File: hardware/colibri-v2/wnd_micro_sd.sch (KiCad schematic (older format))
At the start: 12 parts

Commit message: Added footprints
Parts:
- removed MSD1: uSDCARD-H1.85, symbol uSDCARD-H1.85
- added MSD1: WURTH_693071010811, Sigmadrone:WURTH_693071010811, symbol WURTH_693071010811
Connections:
- wire segments 40 -> 37
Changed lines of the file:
@@
 $Descr A4 11693 8268
 encoding utf-8
-Sheet 13 28
+Sheet 12 28
 Title ""
 Date ""
@@
 Comment4 ""
 $EndDescr
-$Comp
-L uSDCARD-H1.85 MSD1
-U 1 1 56153956
-P 6350 4000
-F 0 "MSD1" H 6600 3300 60  0000 C CNN
-F 1 "uSDCARD-H1.85" H 6450 4700 60  0000 C CNN
-F 2 "" H 6350 4000 60  0001 C CNN
-F 3 "" H 6350 4000 60  0000 C CNN
-	1    6350 4000
-	1    0    0    -1
-$EndComp
 Text HLabel 3450 3450 0    60   BiDi ~ 0
 SD1_DATA2
@@
 SD1_WP
 $Comp
-L GND #PWR108
+L GND #PWR0114
 U 1 1 5617363A
 P 5350 5200
-F 0 "#PWR108" H 5350 4950 50  0001 C CNN
+F 0 "#PWR0114" H 5350 4950 50  0001 C CNN
 F 1 "GND" H 5350 5050 50  0000 C CNN
 F 2 "" H 5350 5200 60  0000 C CNN
@@
 	1    0    0    -1
 $EndComp
-$Comp
-L GND #PWR109
-U 1 1 5617364F
-P 6100 5200
-F 0 "#PWR109" H 6100 4950 50  0001 C CNN
-F 1 "GND" H 6100 5050 50  0000 C CNN
-F 2 "" H 6100 5200 60  0000 C CNN
-F 3 "" H 6100 5200 60  0000 C CNN
-	1    6100 5200
-	1    0    0    -1
-$EndComp
 Wire Wire Line
 	5500 4550 5350 4550
 Wire Wire Line
 	5350 3950 5350 5200
-Wire Wire Line
-	6100 4850 6100 5200
-Wire Wire Line
-	6200 4850 6200 4950
-Wire Wire Line
-	6200 4950 6100 4950
-Connection ~ 6100 4950
 Wire Wire Line
 	3450 3450 5500 3450
@@
 	3800 3850 3450 3850
 $Comp
-L +3V3 #PWR107
+L +3V3 #PWR0115
 U 1 1 561737FF
 P 5350 1550
-F 0 "#PWR107" H 5350 1400 50  0001 C CNN
+F 0 "#PWR0115" H 5350 1400 50  0001 C CNN
 F 1 "+3V3" H 5350 1690 50  0000 C CNN
 F 2 "" H 5350 1550 60  0000 C CNN
@@
 	4200 4450 4200 4600
 $Comp
-L GND #PWR106
+L GND #PWR0116
 U 1 1 56173E31
 P 4200 5200
-F 0 "#PWR106" H 4200 4950 50  0001 C CNN
+F 0 "#PWR0116" H 4200 4950 50  0001 C CNN
 F 1 "GND" H 4200 5050 50  0000 C CNN
 F 2 "" H 4200 5200 60  0000 C CNN
@@
 Connection ~ 4900 1850
 $Comp
-L GND #PWR110
+L GND #PWR0117
 U 1 1 5617463C
 P 6500 2850
-F 0 "#PWR110" H 6500 2600 50  0001 C CNN
+F 0 "#PWR0117" H 6500 2600 50  0001 C CNN
 F 1 "GND" H 6500 2700 50  0000 C CNN
 F 2 "" H 6500 2850 60  0000 C CNN
@@
 	5500 4450 5350 4450
 Connection ~ 5350 4450
+$Comp
+L WURTH_693071010811 MSD1
+U 1 1 56D6C0E1
+P 6350 4000
+F 0 "MSD1" H 6600 3300 60  0000 C CNN
+F 1 "WURTH_693071010811" H 6450 4700 60  0000 C CNN
+F 2 "Sigmadrone:WURTH_693071010811" H 6350 4000 60  0001 C CNN
+F 3 "" H 6600 3300 60  0000 C CNN
+F 4 "2081363" H 6400 4900 60  0001 C CNN "Part"
+F 5 "Farnell" H 6400 4800 60  0001 C CNN "Provider"
+	1    6350 4000
+	1    0    0    -1
+$EndComp
 $EndSCHEMATC

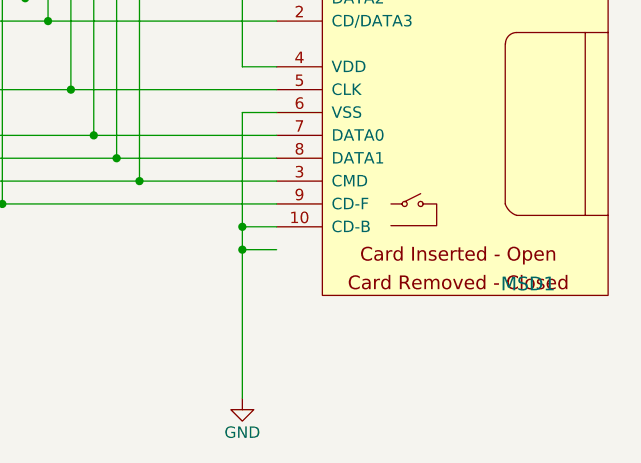
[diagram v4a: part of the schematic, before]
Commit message: Added SPPJ320600.kicad_mod
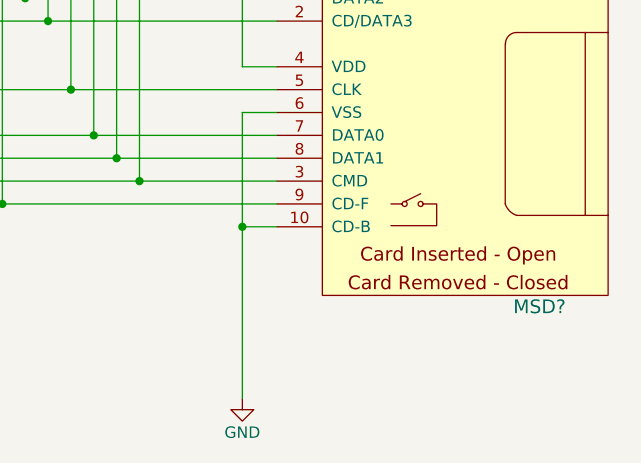
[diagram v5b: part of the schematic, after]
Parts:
- removed MSD1: WURTH_693071010811, Sigmadrone:WURTH_693071010811, symbol WURTH_693071010811
- added MSD?: WURTH_693071010811, symbol WURTH_693071010811
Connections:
- net +3V3: now also MSD?.4 (VDD)
- net GND: now also MSD?.10 (CD-B), MSD?.6 (VSS)
- net SD1_CD: now also MSD?.9 (CD-F)
- net SD1_CMD: now also MSD?.3 (CMD)
- net SD1_DATA0: now also MSD?.7 (DATA0)
- net SD1_DATA1: now also MSD?.8 (DATA1)
- net SD1_DATA2: now also MSD?.1 (DATA2)
- net SD1_DATA3: now also MSD?.2 (CD/DATA3)
- net at R75.1, R80.2: now also MSD?.5 (CLK)
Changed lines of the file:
@@
 $EndComp
-Wire Wire Line
-	5500 4550 5350 4550
 Wire Wire Line
 	5350 3950 5350 5200
@@
 Wire Wire Line
 	5500 3950 5350 3950
-Connection ~ 5350 4550
 Wire Wire Line
 	4100 3850 5500 3850
@@
 Connection ~ 5350 4450
 $Comp
-L WURTH_693071010811 MSD1
-U 1 1 56D6C0E1
+L WURTH_693071010811 MSD?
+U 1 1 56D7C098
 P 6350 4000
-F 0 "MSD1" H 6600 3300 60  0000 C CNN
+F 0 "MSD?" H 6650 3200 60  0000 C CNN
 F 1 "WURTH_693071010811" H 6450 4700 60  0000 C CNN
-F 2 "Sigmadrone:WURTH_693071010811" H 6350 4000 60  0001 C CNN
+F 2 "" H 6350 4000 60  0000 C CNN
 F 3 "" H 6600 3300 60  0000 C CNN
 F 4 "2081363" H 6400 4900 60  0001 C CNN "Part"

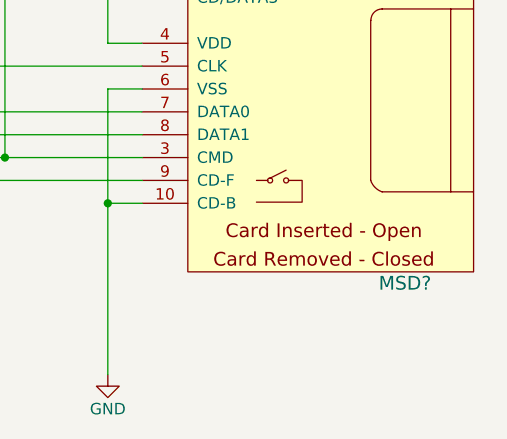
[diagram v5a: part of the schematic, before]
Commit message: Added VL_1220.kicad_mod footprint
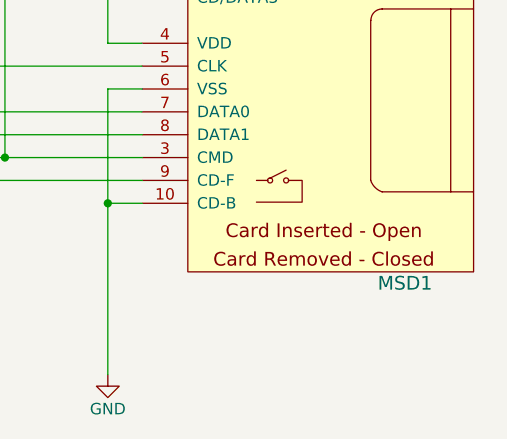
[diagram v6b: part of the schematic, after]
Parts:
- gave numbers to parts that had none: 1
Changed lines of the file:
@@
 SD1_WP
 $Comp
-L GND #PWR0114
+L GND #PWR0115
 U 1 1 5617363A
 P 5350 5200
-F 0 "#PWR0114" H 5350 4950 50  0001 C CNN
+F 0 "#PWR0115" H 5350 4950 50  0001 C CNN
 F 1 "GND" H 5350 5050 50  0000 C CNN
 F 2 "" H 5350 5200 60  0000 C CNN
@@
 	3800 3850 3450 3850
 $Comp
-L +3V3 #PWR0115
+L +3V3 #PWR0116
 U 1 1 561737FF
 P 5350 1550
-F 0 "#PWR0115" H 5350 1400 50  0001 C CNN
+F 0 "#PWR0116" H 5350 1400 50  0001 C CNN
 F 1 "+3V3" H 5350 1690 50  0000 C CNN
 F 2 "" H 5350 1550 60  0000 C CNN
@@
 	4200 4450 4200 4600
 $Comp
-L GND #PWR0116
+L GND #PWR0117
 U 1 1 56173E31
 P 4200 5200
-F 0 "#PWR0116" H 4200 4950 50  0001 C CNN
+F 0 "#PWR0117" H 4200 4950 50  0001 C CNN
 F 1 "GND" H 4200 5050 50  0000 C CNN
 F 2 "" H 4200 5200 60  0000 C CNN
@@
 Connection ~ 4900 1850
 $Comp
-L GND #PWR0117
+L GND #PWR0118
 U 1 1 5617463C
 P 6500 2850
-F 0 "#PWR0117" H 6500 2600 50  0001 C CNN
+F 0 "#PWR0118" H 6500 2600 50  0001 C CNN
 F 1 "GND" H 6500 2700 50  0000 C CNN
 F 2 "" H 6500 2850 60  0000 C CNN
@@
 Connection ~ 5350 4450
 $Comp
-L WURTH_693071010811 MSD?
+L WURTH_693071010811 MSD1
 U 1 1 56D7C098
 P 6350 4000
-F 0 "MSD?" H 6650 3200 60  0000 C CNN
+F 0 "MSD1" H 6650 3200 60  0000 C CNN
 F 1 "WURTH_693071010811" H 6450 4700 60  0000 C CNN
 F 2 "" H 6350 4000 60  0000 C CNN

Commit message: Added AP6681GMT-HF-3.kicad_mod. Fixed netlist errors
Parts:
- MSD1: footprint (none) -> Sigmadrone:WURTH_693071010811
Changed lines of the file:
@@
 F 0 "MSD1" H 6650 3200 60  0000 C CNN
 F 1 "WURTH_693071010811" H 6450 4700 60  0000 C CNN
-F 2 "" H 6350 4000 60  0000 C CNN
+F 2 "Sigmadrone:WURTH_693071010811" H 6350 4000 60  0001 C CNN
 F 3 "" H 6600 3300 60  0000 C CNN
 F 4 "2081363" H 6400 4900 60  0001 C CNN "Part"
